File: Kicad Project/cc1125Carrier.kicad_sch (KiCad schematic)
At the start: 7 parts, among them J1 TFM-110-02-SM-D-A-K-TR, J2 TFM-110-02-SM-D-A-K-TR, J3 Jumper Block, J4 Conn_01x06, U1 YAAJ_WeAct_BlackPill_Part_Lik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

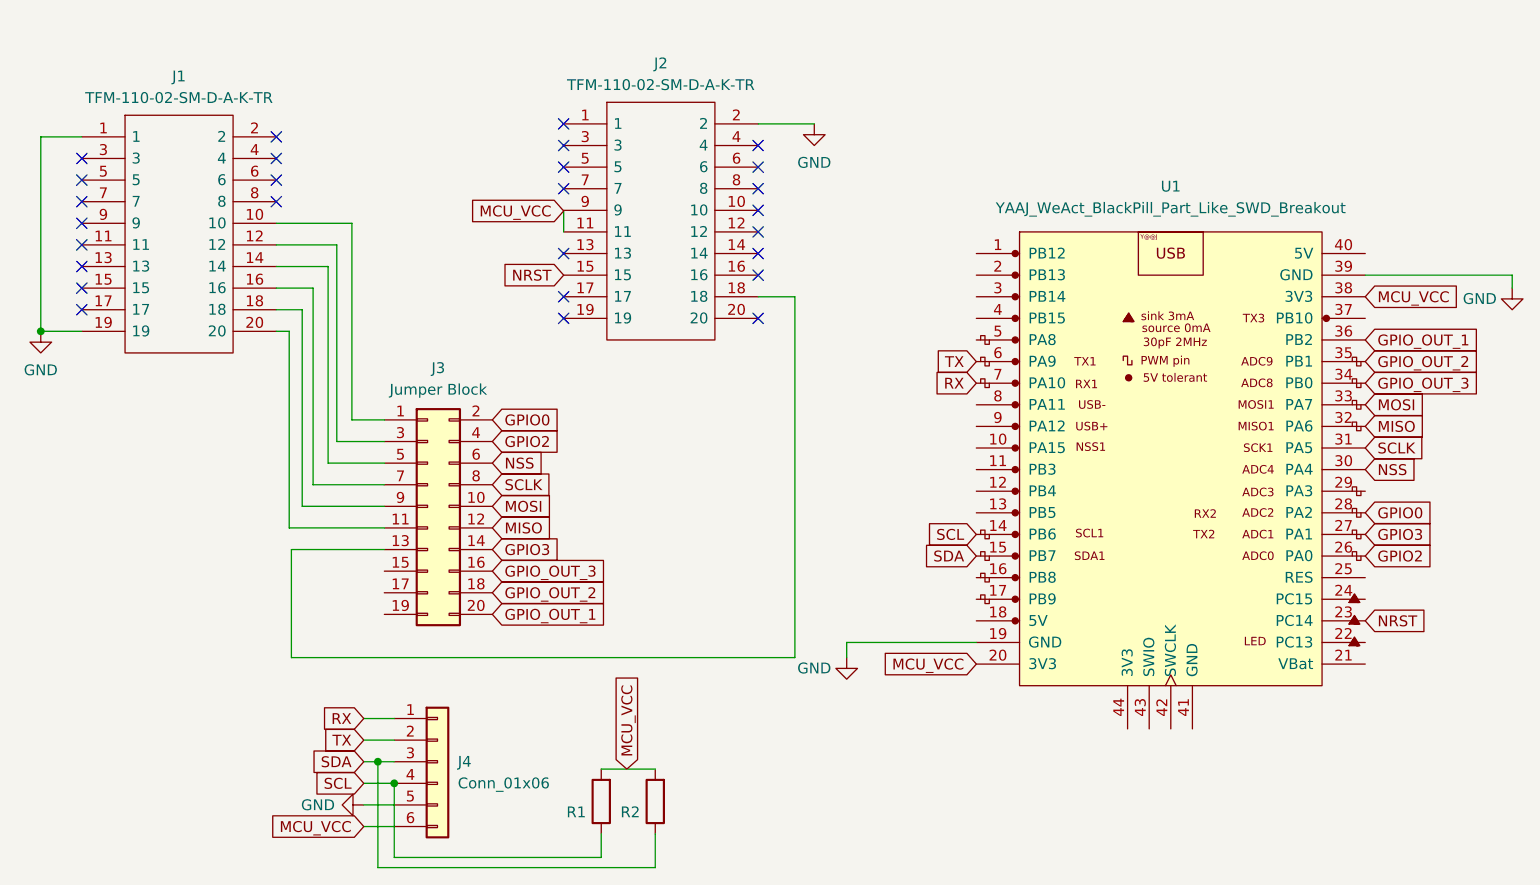
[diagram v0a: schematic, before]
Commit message: add STM project & re-arrange to include it
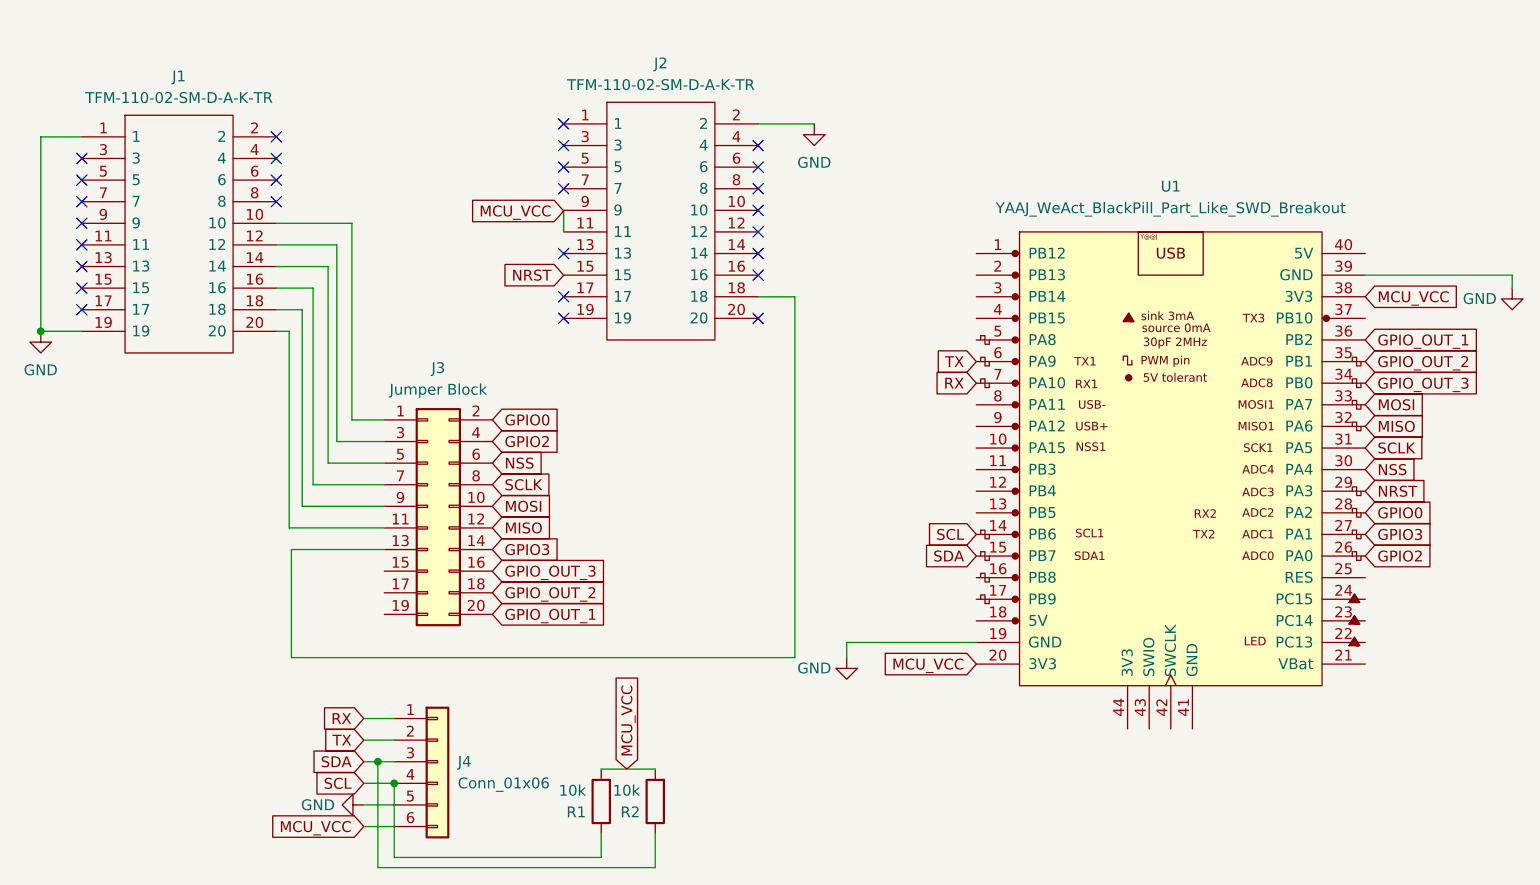
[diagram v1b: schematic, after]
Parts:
- R1, R2: value (none) -> 10k; footprint (none) -> Resistor_SMD:R_0402_1005Metric
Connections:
- net NRST: now also U1.29 (PA3); no longer U1.23 (PC14)
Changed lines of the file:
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@@
+    )
+  )
+  (global_label "NRST" (shape input) (at 218.44 112.268 0) (fields_autoplaced)
+    (effects (font (size 1.27 1.27)) (justify left))
+    (property "Intersheet References" "${INTERSHEET_REFS}" (id 0) (at 225.6307 112.3474 0)
+      (effects (font (size 1.27 1.27)) (justify left) hide)
     )
   )
@@
     (effects (font (size 1.27 1.27)) (justify left))
     (property "Intersheet References" "${INTERSHEET_REFS}" (id 0) (at 232.1017 96.9486 0)
-      (effects (font (size 1.27 1.27)) (justify left) hide)
-    )
-  )
-  (global_label "NRST" (shape input) (at 218.44 127.508 0) (fields_autoplaced)
-    (effects (font (size 1.27 1.27)) (justify left))
-    (property "Intersheet References" "${INTERSHEET_REFS}" (id 0) (at 225.6307 127.5874 0)
       (effects (font (size 1.27 1.27)) (justify left) hide)
     )
@@
       (effects (font (size 1.27 1.27)) (justify left))
     )
-    (property "Value" "" (id 1) (at 126.8476 147.4725 0)
-      (effects (font (size 1.27 1.27)) (justify left))
-    )
-    (property "Footprint" "" (id 2) (at 130.4036 148.7424 90)
+    (property "Value" "10k" (id 1) (at 126.8476 147.4725 0)
+      (effects (font (size 1.27 1.27)) (justify left))
+    )
+    (property "Footprint" "Resistor_SMD:R_0402_1005Metric" (id 2) (at 130.4036 148.7424 90)
       (effects (font (size 1.27 1.27)) hide)
     )
@@
       (effects (font (size 1.27 1.27)) (justify left))
     )
-    (property "Value" "" (id 1) (at 133.1976 147.4725 0)
-      (effects (font (size 1.27 1.27)) (justify left))
-    )
-    (property "Footprint" "" (id 2) (at 136.7536 148.7424 90)
-      (effects (font (size 1.27 1.27)) hide)
-    )
+    (property "Value" "10k" (id 1) (at 133.1976 147.4725 0)
+      (effects (font (size 1.27 1.27)) (justify left))
+    )
+    (property "Footprint" "Resistor_SMD:R_0402_1005Metric" (id 2) (at 136.7536 148.7424 90)
+      (effects (font (size 1.27 1.27)) hide)
+    )

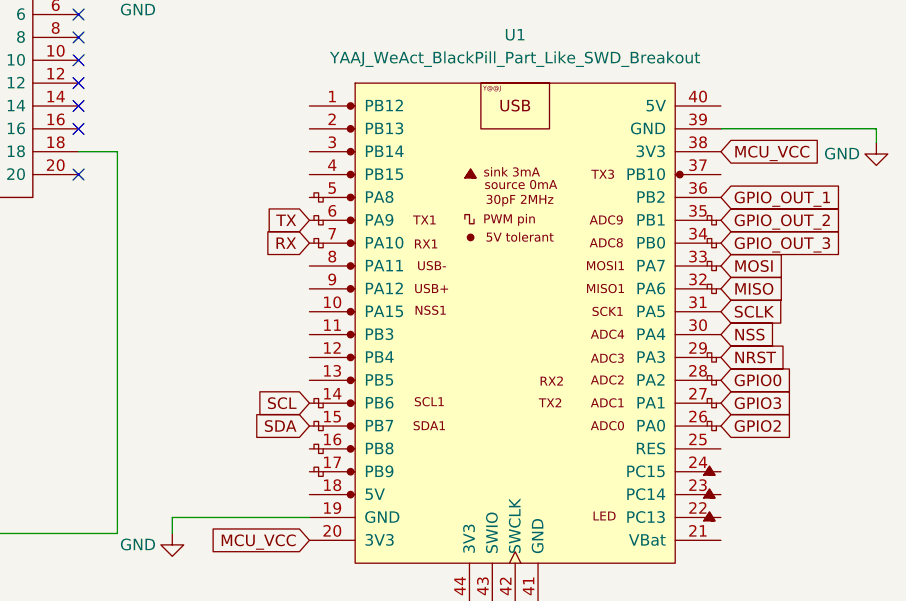
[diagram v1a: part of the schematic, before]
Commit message: move signals off of PA0 and PB2 due to conflict with stm32 buttons
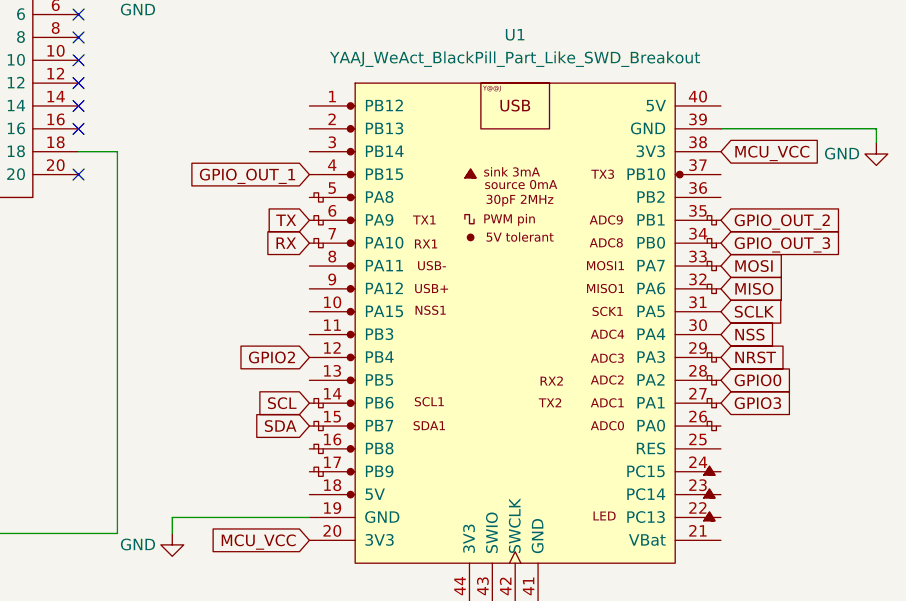
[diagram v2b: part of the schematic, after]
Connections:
- net GPIO2: now also U1.12 (PB4); no longer U1.26 (PA0)
- net GPIO_OUT_1: now also U1.4 (PB15); no longer U1.36 (PB2)
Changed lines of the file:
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@@
     )
   )
-  (global_label "GPIO2" (shape input) (at 218.44 119.888 0) (fields_autoplaced)
-    (effects (font (size 1.27 1.27)) (justify left))
-    (property "Intersheet References" "${INTERSHEET_REFS}" (id 0) (at 226.5379 119.8086 0)
-      (effects (font (size 1.27 1.27)) (justify left) hide)
+  (global_label "GPIO2" (shape input) (at 172.72 112.268 180) (fields_autoplaced)
+    (effects (font (size 1.27 1.27)) (justify right))
+    (property "Intersheet References" "${INTERSHEET_REFS}" (id 0) (at 164.6221 112.3474 0)
+      (effects (font (size 1.27 1.27)) (justify right) hide)
     )
   )
@@
     )
   )
-  (global_label "GPIO_OUT_1" (shape input) (at 218.44 94.488 0) (fields_autoplaced)
-    (effects (font (size 1.27 1.27)) (justify left))
-    (property "Intersheet References" "${INTERSHEET_REFS}" (id 0) (at 232.1017 94.4086 0)
-      (effects (font (size 1.27 1.27)) (justify left) hide)
+  (global_label "GPIO_OUT_1" (shape input) (at 172.72 91.948 180) (fields_autoplaced)
+    (effects (font (size 1.27 1.27)) (justify right))
+    (property "Intersheet References" "${INTERSHEET_REFS}" (id 0) (at 159.0583 92.0274 0)
+      (effects (font (size 1.27 1.27)) (justify right) hide)
     )
   )

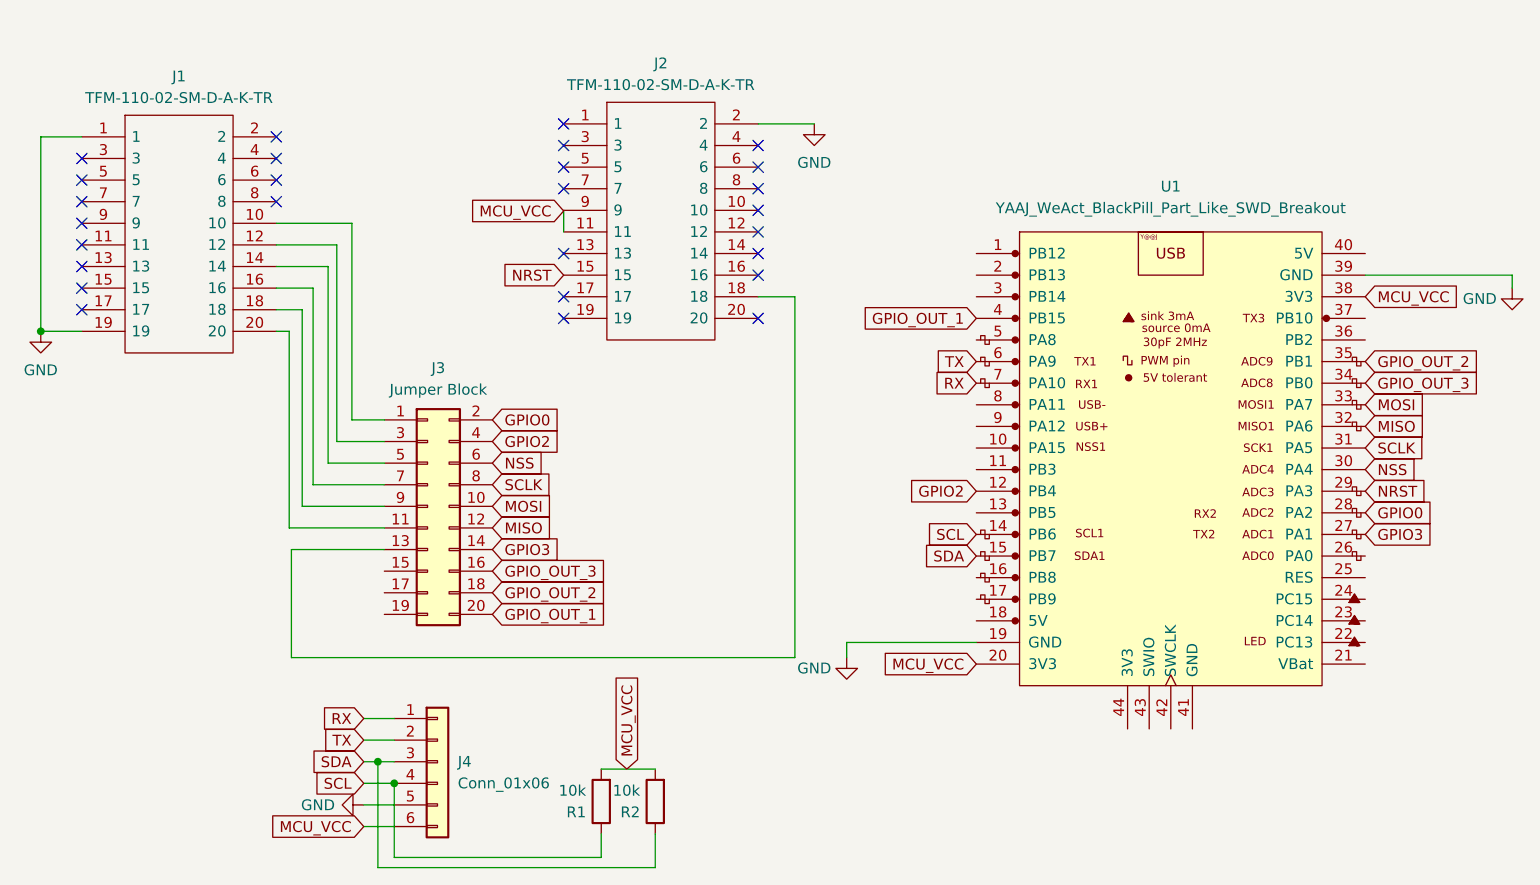
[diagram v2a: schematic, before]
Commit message: add emk daughter board symbol and footprint
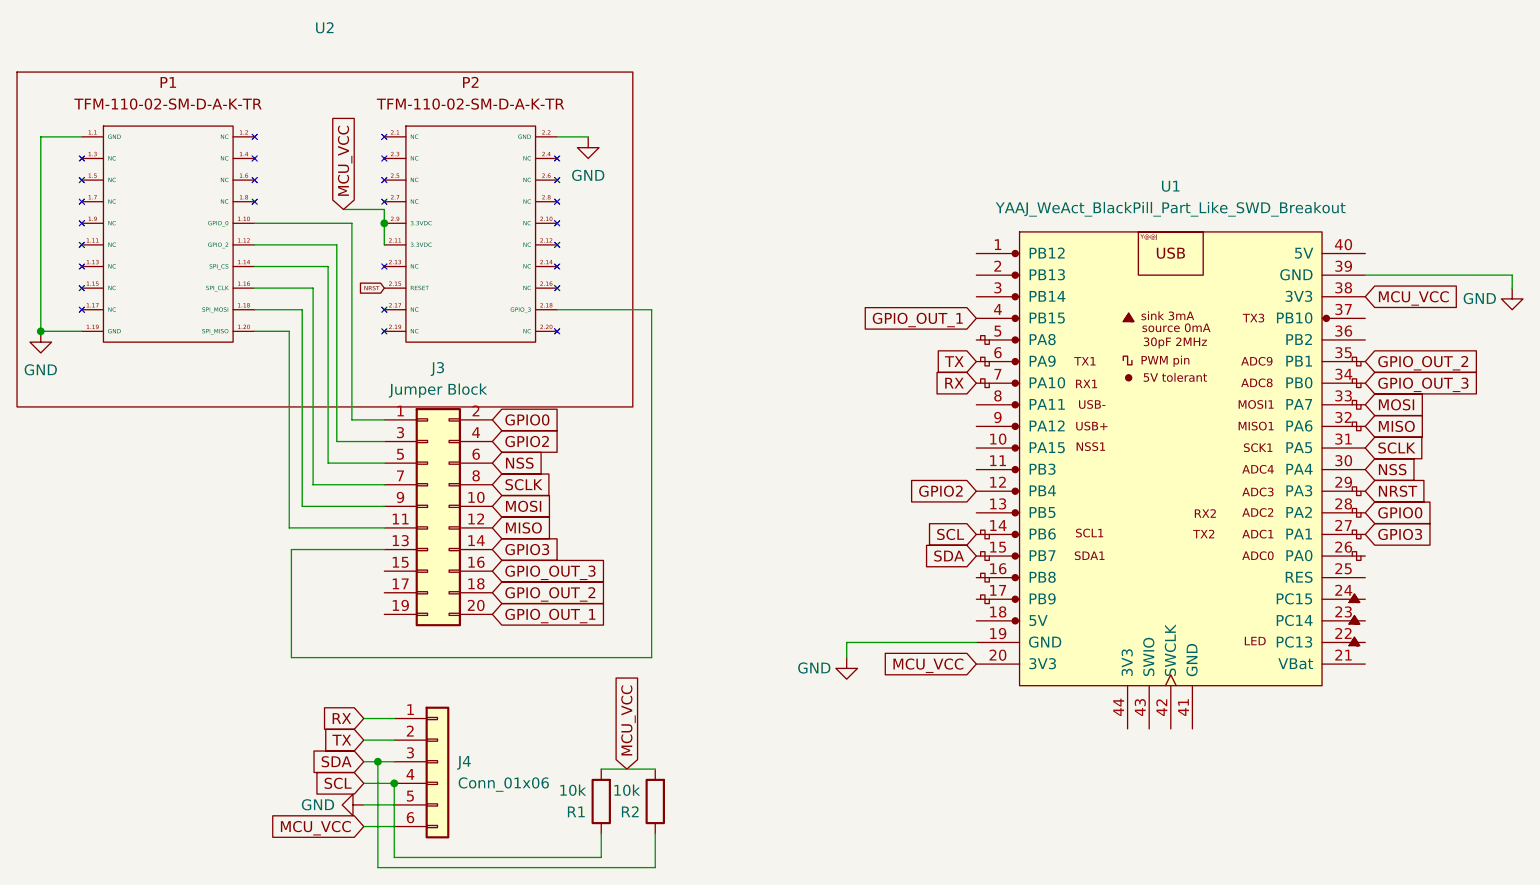
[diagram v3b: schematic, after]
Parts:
- removed J1, J2: TFM-110-02-SM-D-A-K-TR, SamacSys_Parts:TFM-110-02-XXX-D-A-Y-TR, symbol SamacSys_Parts:TFM-110-02-SM-D-A-K-TR
- added U2: (no value), symbol RF_TI:TI CC112X EMK Daughter Board
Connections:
- net GND: now also U2.1.1 (GND), U2.1.19 (GND), U2.2.2 (GND)
- net MCU_VCC: now also U2.2.11 (3.3VDC), U2.2.9 (3.3VDC)
- net NRST: now also U2.2.15 (RESET)
- net at J3.1 (Pin_1): now also U2.1.10 (GPIO_0)
- net at J3.11 (Pin_11): now also U2.1.20 (SPI_MISO)
- net at J3.13 (Pin_13): now also U2.2.18 (GPIO_3)
- net at J3.3 (Pin_3): now also U2.1.12 (GPIO_2)
- net at J3.5 (Pin_5): now also U2.1.14 (SPI_CS)
- net at J3.7 (Pin_7): now also U2.1.16 (SPI_CLK)
- net at J3.9 (Pin_9): now also U2.1.18 (SPI_MOSI)
- no-connect marks 27 -> 0
